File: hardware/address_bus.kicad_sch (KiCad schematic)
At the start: 17 parts, among them Q7 BC557, Q8 BC557, U2 74LS06N, U5 74HC595, U6 74HC595, U7 74HC595

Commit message: Rev.E. Updated specifications document and hardware design.
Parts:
- Q7, Q8: value BC557 -> (none); footprint Package_TO_SOT_THT:TO-92_Inline_Wide -> (none)
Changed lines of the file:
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@@
       (effects (font (size 1.27 1.27)) (justify left))
     )
-    (property "Value" "BC557" (id 1) (at 185.1914 77.343 0)
+    (property "Value" "" (id 1) (at 185.1914 77.343 0)
       (effects (font (size 1.27 1.27)) (justify left))
     )
-    (property "Footprint" "Package_TO_SOT_THT:TO-92_Inline_Wide" (id 2) (at 185.42 74.295 0)
+    (property "Footprint" "" (id 2) (at 185.42 74.295 0)
       (effects (font (size 1.27 1.27) italic) (justify left) hide)
     )
@@
       (effects (font (size 1.27 1.27)) (justify left))
     )
-    (property "Value" "BC557" (id 1) (at 185.1914 123.063 0)
+    (property "Value" "" (id 1) (at 185.1914 123.063 0)
       (effects (font (size 1.27 1.27)) (justify left))
     )
-    (property "Footprint" "Package_TO_SOT_THT:TO-92_Inline_Wide" (id 2) (at 185.42 120.015 0)
+    (property "Footprint" "" (id 2) (at 185.42 120.015 0)
       (effects (font (size 1.27 1.27) italic) (justify left) hide)
     )

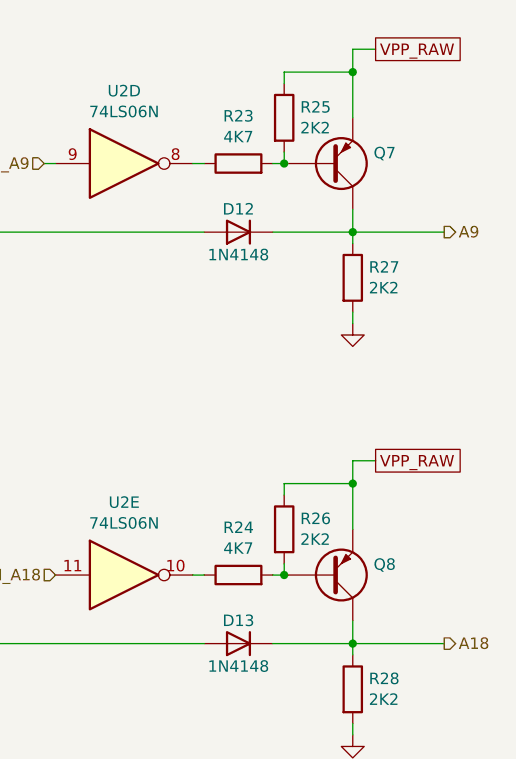
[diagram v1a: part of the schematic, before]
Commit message: Rev.E. Updated R51 wattage.
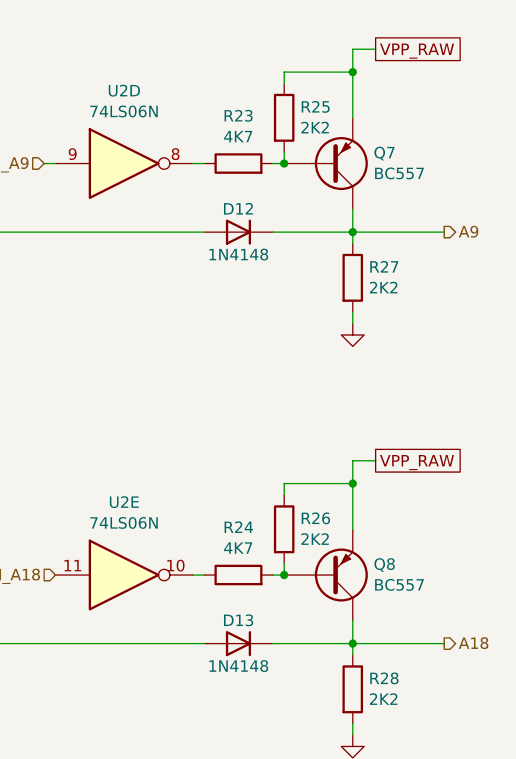
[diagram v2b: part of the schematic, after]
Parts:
- Q7, Q8: value (none) -> BC557; footprint (none) -> Package_TO_SOT_THT:TO-92_Inline_Wide
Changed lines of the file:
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@@
       (effects (font (size 1.27 1.27)) (justify left))
     )
-    (property "Value" "" (id 1) (at 185.1914 77.343 0)
+    (property "Value" "BC557" (id 1) (at 185.1914 77.343 0)
       (effects (font (size 1.27 1.27)) (justify left))
     )
-    (property "Footprint" "" (id 2) (at 185.42 74.295 0)
+    (property "Footprint" "Package_TO_SOT_THT:TO-92_Inline_Wide" (id 2) (at 185.42 74.295 0)
       (effects (font (size 1.27 1.27) italic) (justify left) hide)
     )
@@
       (effects (font (size 1.27 1.27)) (justify left))
     )
-    (property "Value" "" (id 1) (at 185.1914 123.063 0)
+    (property "Value" "BC557" (id 1) (at 185.1914 123.063 0)
       (effects (font (size 1.27 1.27)) (justify left))
     )
-    (property "Footprint" "" (id 2) (at 185.42 120.015 0)
+    (property "Footprint" "Package_TO_SOT_THT:TO-92_Inline_Wide" (id 2) (at 185.42 120.015 0)
       (effects (font (size 1.27 1.27) italic) (justify left) hide)
     )
